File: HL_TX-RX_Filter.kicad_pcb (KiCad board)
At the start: 2 copper layers, 100 x 100 mm, 184 parts, among them J1 To Antenna, J2 From Tx, J3 ICSP, J4 Data In, J5 SCL SDA, J6 To Rx in, Q1 2N7002, Q2 2N7002, Q3 2N7002, Q4 2N7002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

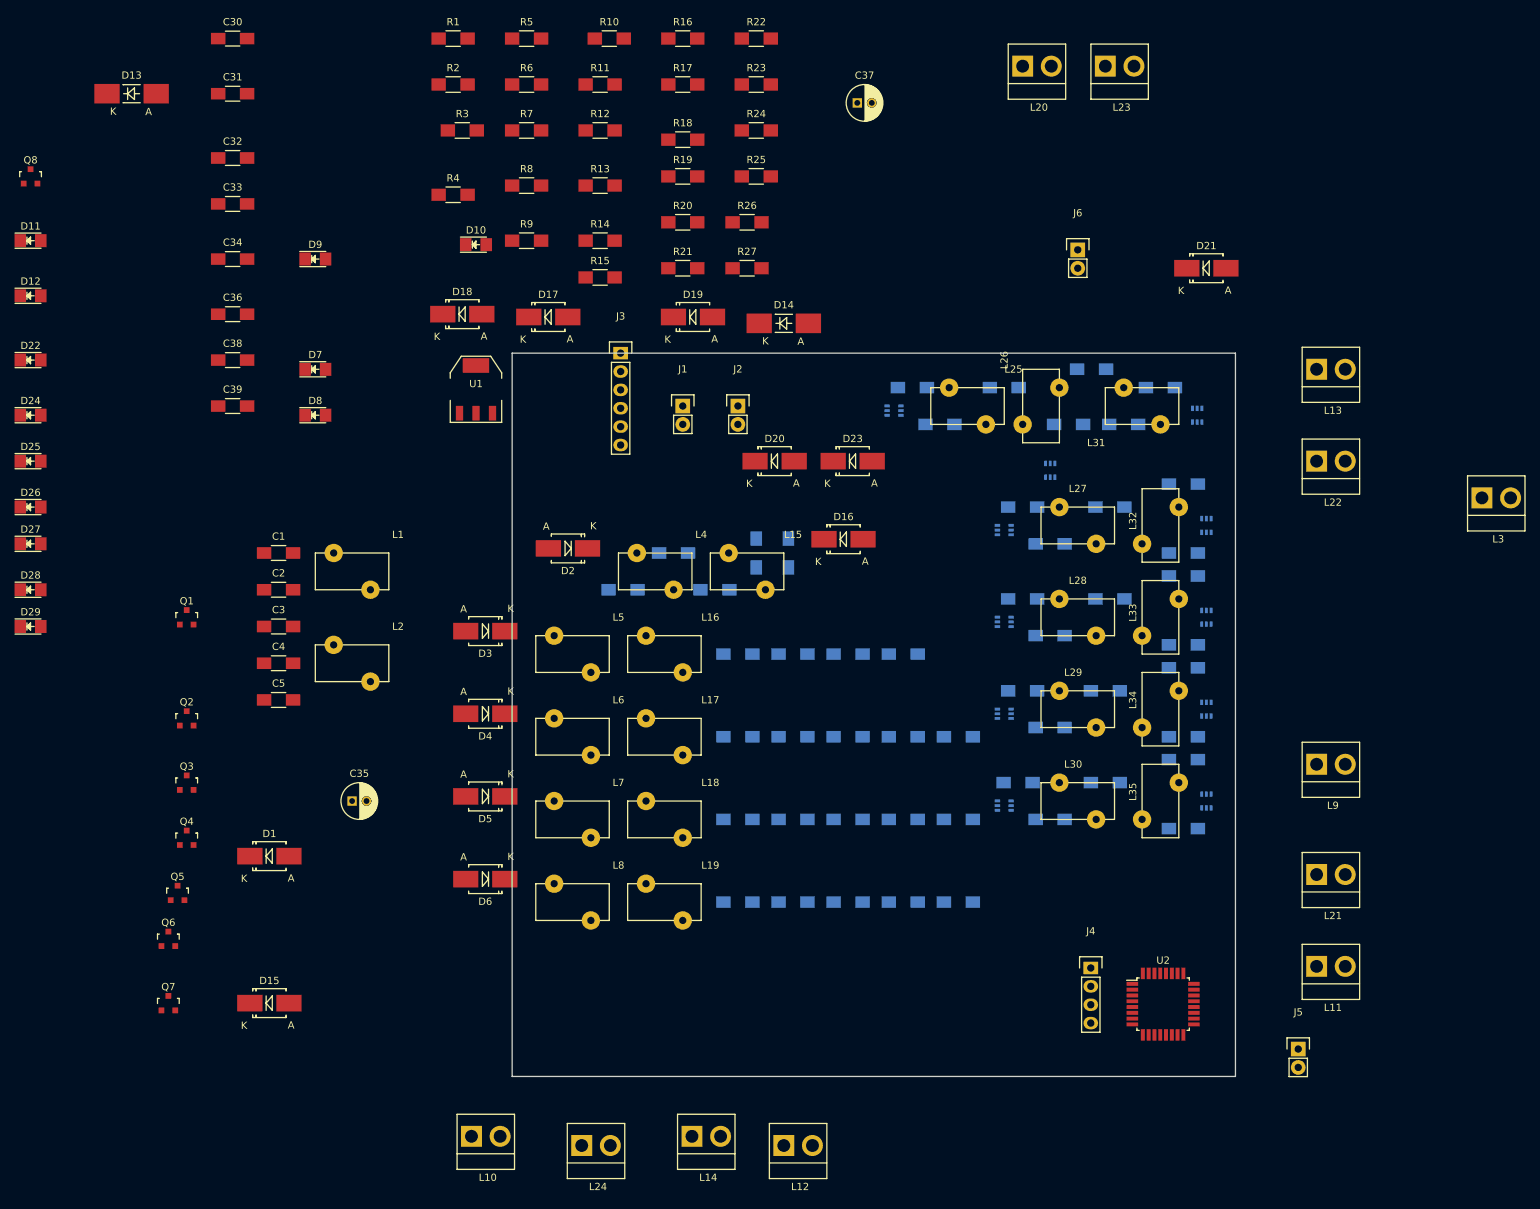
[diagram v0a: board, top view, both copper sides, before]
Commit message: Resized toroids and M7 diodes
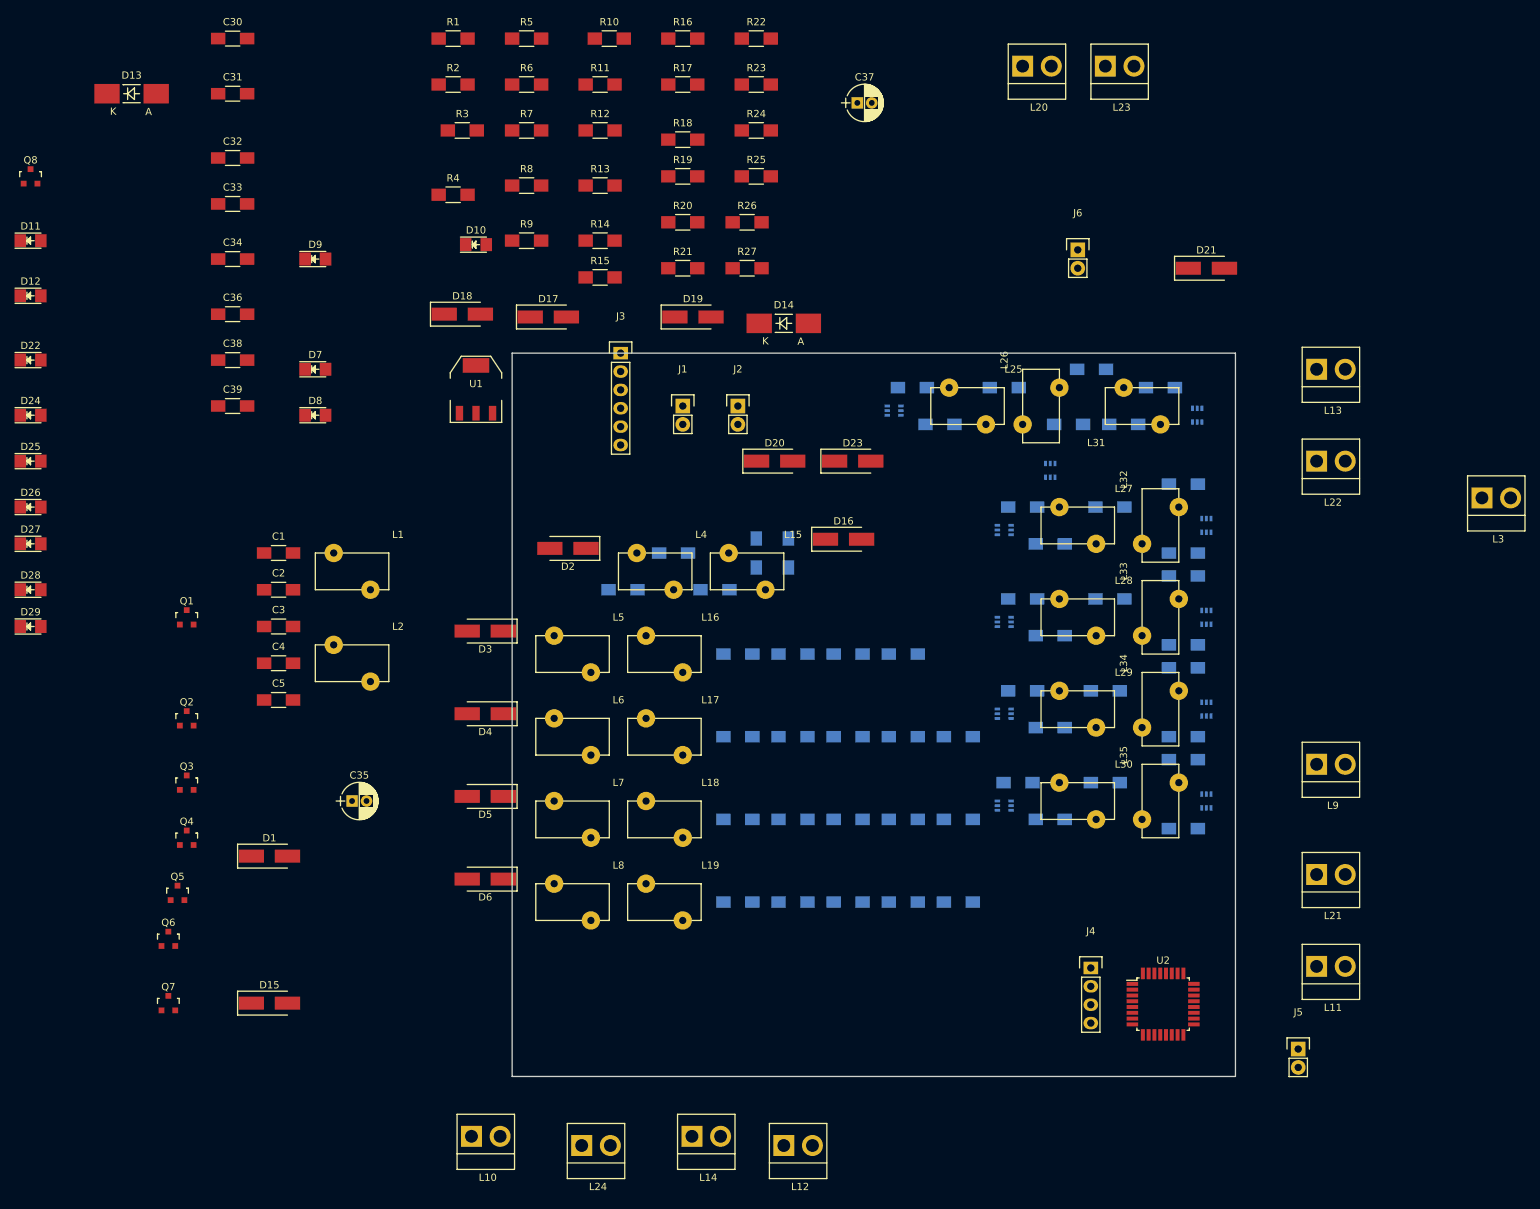
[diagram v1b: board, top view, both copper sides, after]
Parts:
- C35, C37: footprint Capacitors_ThroughHole:C_Radial_D5_L11_P2 -> Capacitors_THT:CP_Radial_D5.0mm_P2.00mm
- D1, D15, D16, D17, D18, D19, D2, D20, D21, D23, D3, D4, D5, D6: footprint Diodes_SMD:SMB_Handsoldering -> Diodes_SMD:D_SMA_Handsoldering
- L1, L15, L16, L17, L18, L19, L2, L25, L26, L27, L28, L29, L30, L31, L32, L33, L34, L35, L4, L5, L6, L7, L8: footprint Inductors:Toroid_T37_Vertical -> Inductors_G:Toroid_T37_Vertical

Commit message: Work on Tx Filter layout
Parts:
- moved C20 42.7 mm to (167.6, 144.1)
- moved C10 42.5 mm to (156.8, 144.1)
- moved C17 35.3 mm to (153.7, 105.4)
- moved C7 34.4 mm to (140.3, 105.4), turned to 180 degrees
- moved C15 16.6 mm to (147.3, 100.3)
- moved D3 11.6 mm to (132.7, 100.3)
- moved L16 11.5 mm to (152.4, 105.4)
- moved L5 11.5 mm to (139.7, 105.4)
- moved C25 3.24 mm to (175.9, 102.2)
- moved C16 0.63 mm to (153.7, 92.7)
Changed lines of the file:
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@@
-(kicad_pcb (version 4) (host pcbnew 4.0.6-e0-6349~53~ubuntu14.04.1)
+(kicad_pcb (version 4) (host pcbnew 4.0.6-e0-6349~53~ubuntu16.04.1)
   (general
     (links 329)
     (no_connects 329)
-    (area 124.924999 59.924999 225.075001 160.075001)
+    (area 55.315238 13.235 265.505001 176.32)
     (thickness 1.6)
     (drawings 4)
@@
   )
   (module Capacitors_SMD:C_1206_HandSoldering placed (layer B.Cu)
-    (at 156.21 135.89)
+    (at 140.335 105.41 180)
     (descr "Capacitor SMD 1206, hand soldering")
     (tags "capacitor 1206")
     (attr smd)
-    (fp_text reference C7 (at 0 2.3) (layer B.SilkS)
+    (fp_text reference C7 (at 0 2.3 180) (layer B.SilkS)
       (effects (font (size 1 1) (thickness 0.15)) (justify mirror))
     )
-    (fp_text value 150p (at 0 -2.3) (layer B.Fab)
+    (fp_text value 150p (at 0 -2.3 180) (layer B.Fab)
       (effects (font (size 1 1) (thickness 0.15)) (justify mirror))
     )
@@
     (fp_line (start 1 1.025) (end -1 1.025) (layer B.SilkS) (width 0.15))
     (fp_line (start -1 -1.025) (end 1 -1.025) (layer B.SilkS) (width 0.15))
-    (pad 1 smd rect (at -2 0) (size 2 1.6) (layers B.Cu B.Paste B.Mask)
+    (pad 1 smd rect (at -2 0 180) (size 2 1.6) (layers B.Cu B.Paste B.Mask)
       (net 6 "Net-(C12-Pad1)"))
-    (pad 2 smd rect (at 2 0) (size 2 1.6) (layers B.Cu B.Paste B.Mask)
+    (pad 2 smd rect (at 2 0 180) (size 2 1.6) (layers B.Cu B.Paste B.Mask)
       (net 4 GND))
     (model Capacitors_SMD.3dshapes/C_1206_HandSoldering.wrl
@@
   )
   (module Capacitors_SMD:C_1206_HandSoldering placed (layer B.Cu)
-    (at 156.21 101.6)
+    (at 156.845 144.145)
     (descr "Capacitor SMD 1206, hand soldering")
     (tags "capacitor 1206")
@@
   )
   (module Capacitors_SMD:C_1206_HandSoldering placed (layer B.Cu)
-    (at 163.83 101.6)
+    (at 147.32 100.33)
     (descr "Capacitor SMD 1206, hand soldering")
     (tags "capacitor 1206")
@@
   )
   (module Capacitors_SMD:C_1206_HandSoldering placed (layer B.Cu)
-    (at 153.035 92.71)
+    (at 153.67 92.71)
     (descr "Capacitor SMD 1206, hand soldering")
     (tags "capacitor 1206")
@@
   )
   (module Capacitors_SMD:C_1206_HandSoldering placed (layer B.Cu)
-    (at 171.45 135.89)
+    (at 153.67 105.41)
     (descr "Capacitor SMD 1206, hand soldering")
     (tags "capacitor 1206")
@@
   )
   (module Capacitors_SMD:C_1206_HandSoldering placed (layer B.Cu)
-    (at 171.45 101.6)
+    (at 167.64 144.145)
     (descr "Capacitor SMD 1206, hand soldering")
     (tags "capacitor 1206")
@@
     (tags "capacitor 1206")
     (attr smd)
-    (fp_text reference C21 (at 0 2.3 90) (layer B.SilkS)
+    (fp_text reference C21 (at -0.635 1.905 90) (layer B.SilkS)
       (effects (font (size 1 1) (thickness 0.15)) (justify mirror))
     )
@@
   )
   (module Capacitors_SMD:C_1206_HandSoldering placed (layer B.Cu)
-    (at 179.07 101.6)
+    (at 175.895 102.235)
     (descr "Capacitor SMD 1206, hand soldering")
     (tags "capacitor 1206")
@@
     (tags "capacitor 1206")
     (attr smd)
-    (fp_text reference C26 (at 0 2.3 270) (layer B.SilkS)
+    (fp_text reference C26 (at 3.175 -2.54 270) (layer B.SilkS)
       (effects (font (size 1 1) (thickness 0.15)) (justify mirror))
     )
@@
   )
   (module Inductors_G:Toroid_T37_Vertical (layer F.Cu)
-    (at 128.27 104.14)
+    (at 139.7 105.41)
     (descr "Toroid, Coil, Choke,  5mm x 10mm, Vertical, Inductor, Drossel, Thruhole,")
     (tags "Toroid, Coil, Choke, 5mm x 10mm, Vertical, Inductor, Drossel, Thruhole,")
@@
   )
   (module Inductors_G:Toroid_T37_Vertical (layer F.Cu)
-    (at 140.97 104.14)
+    (at 152.4 105.41)
     (descr "Toroid, Coil, Choke,  5mm x 10mm, Vertical, Inductor, Drossel, Thruhole,")
     (tags "Toroid, Coil, Choke, 5mm x 10mm, Vertical, Inductor, Drossel, Thruhole,")
@@
   )
   (module Diodes_SMD:D_SMA_Handsoldering (layer F.Cu)
-    (at 121.285 98.425 180)
+    (at 132.715 100.33 180)
     (descr "Diode SMA (DO-214AC) Handsoldering")
     (tags "Diode SMA (DO-214AC) Handsoldering")

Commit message: More Tx filter layout
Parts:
- C30: moved to B.Cu
- moved C30 144.1 mm to (163.2, 138.4), turned to 270 degrees
- moved D18 77.3 mm to (170.8, 111.1)
- moved D19 71.9 mm to (170.8, 123.8)
- moved D20 61.7 mm to (170.8, 135.9)
- moved D17 59.6 mm to (170.8, 98.4)
- moved C27 42.6 mm to (163.2, 100.3), turned to 270 degrees
- moved C22 41.0 mm to (158.8, 100.3), turned to 90 degrees
- moved C25 40.1 mm to (158.8, 138.4), turned to 90 degrees
- moved C12 39.2 mm to (147.3, 100.3)
- moved C15 38.1 mm to (147.3, 138.4)
- moved C29 26.7 mm to (163.2, 125.7), turned to 270 degrees
- moved C28 26.1 mm to (163.2, 113.0), turned to 270 degrees
- moved C19 25.1 mm to (153.7, 130.8)
- moved C24 24.0 mm to (158.8, 125.7), turned to 90 degrees
- moved C9 23.8 mm to (140.3, 130.8), turned to 180 degrees
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
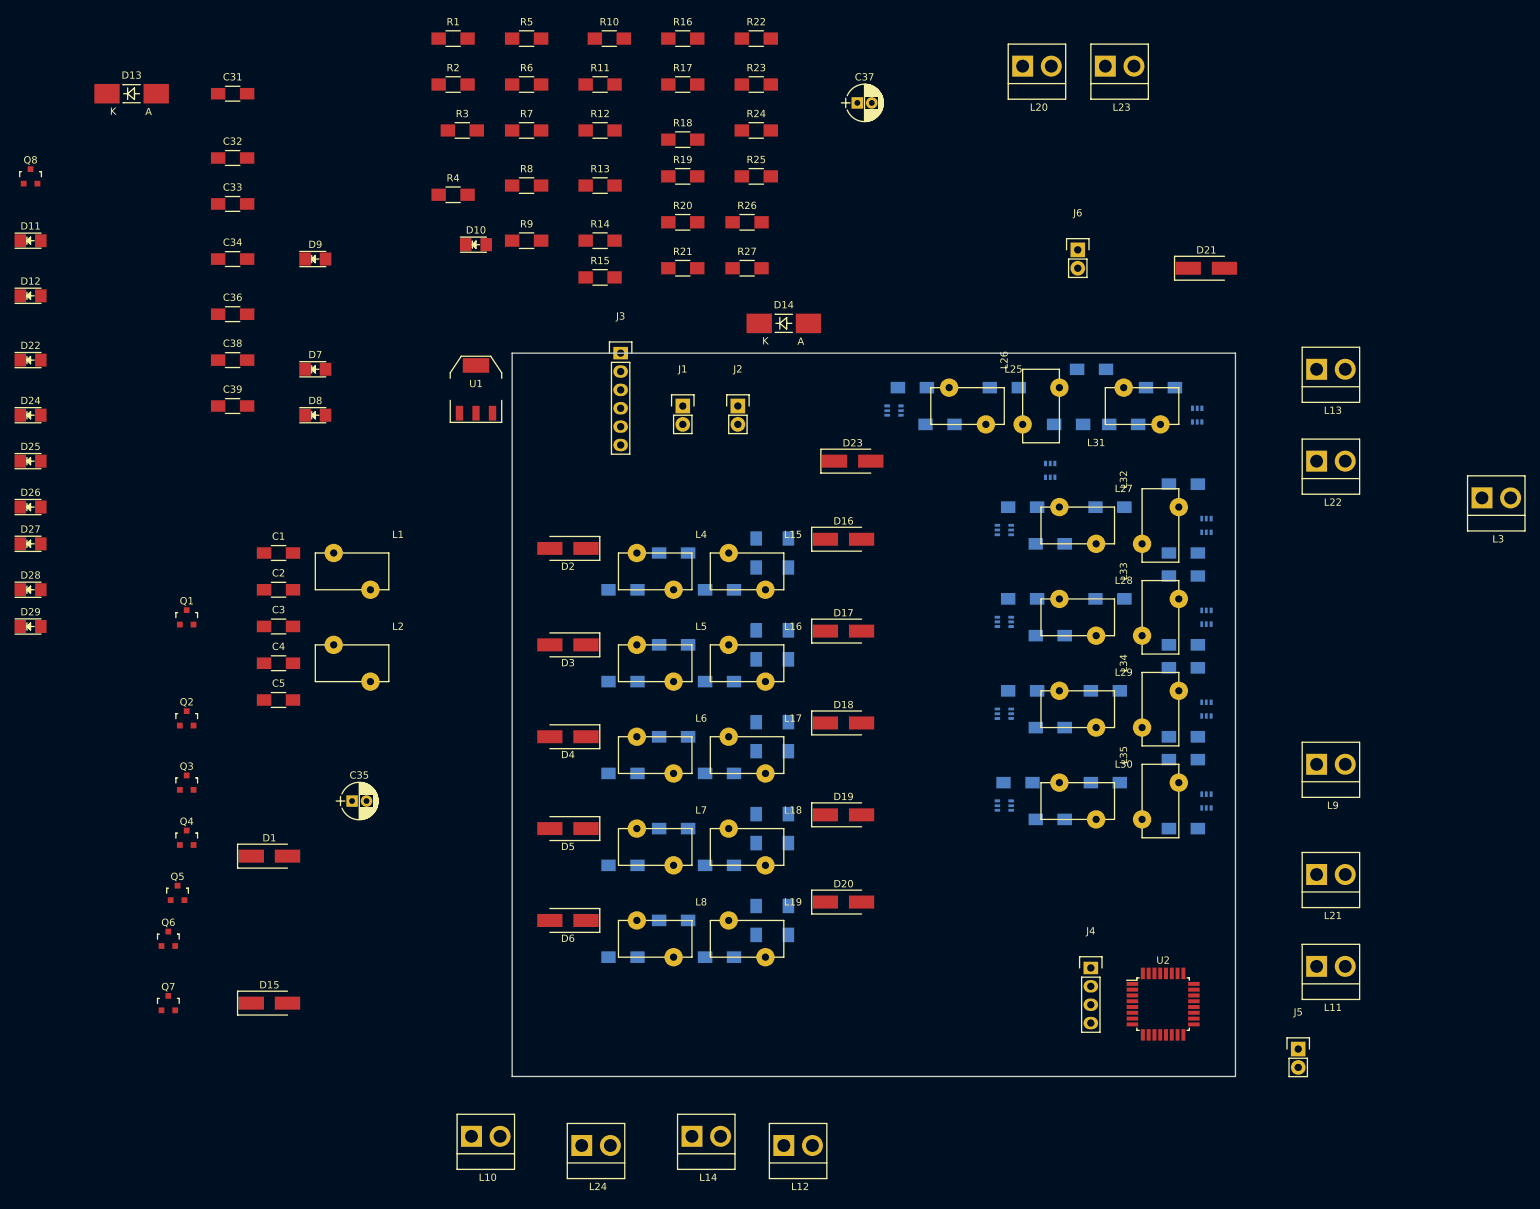
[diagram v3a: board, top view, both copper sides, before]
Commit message: More Tx layout and choke footprint mods
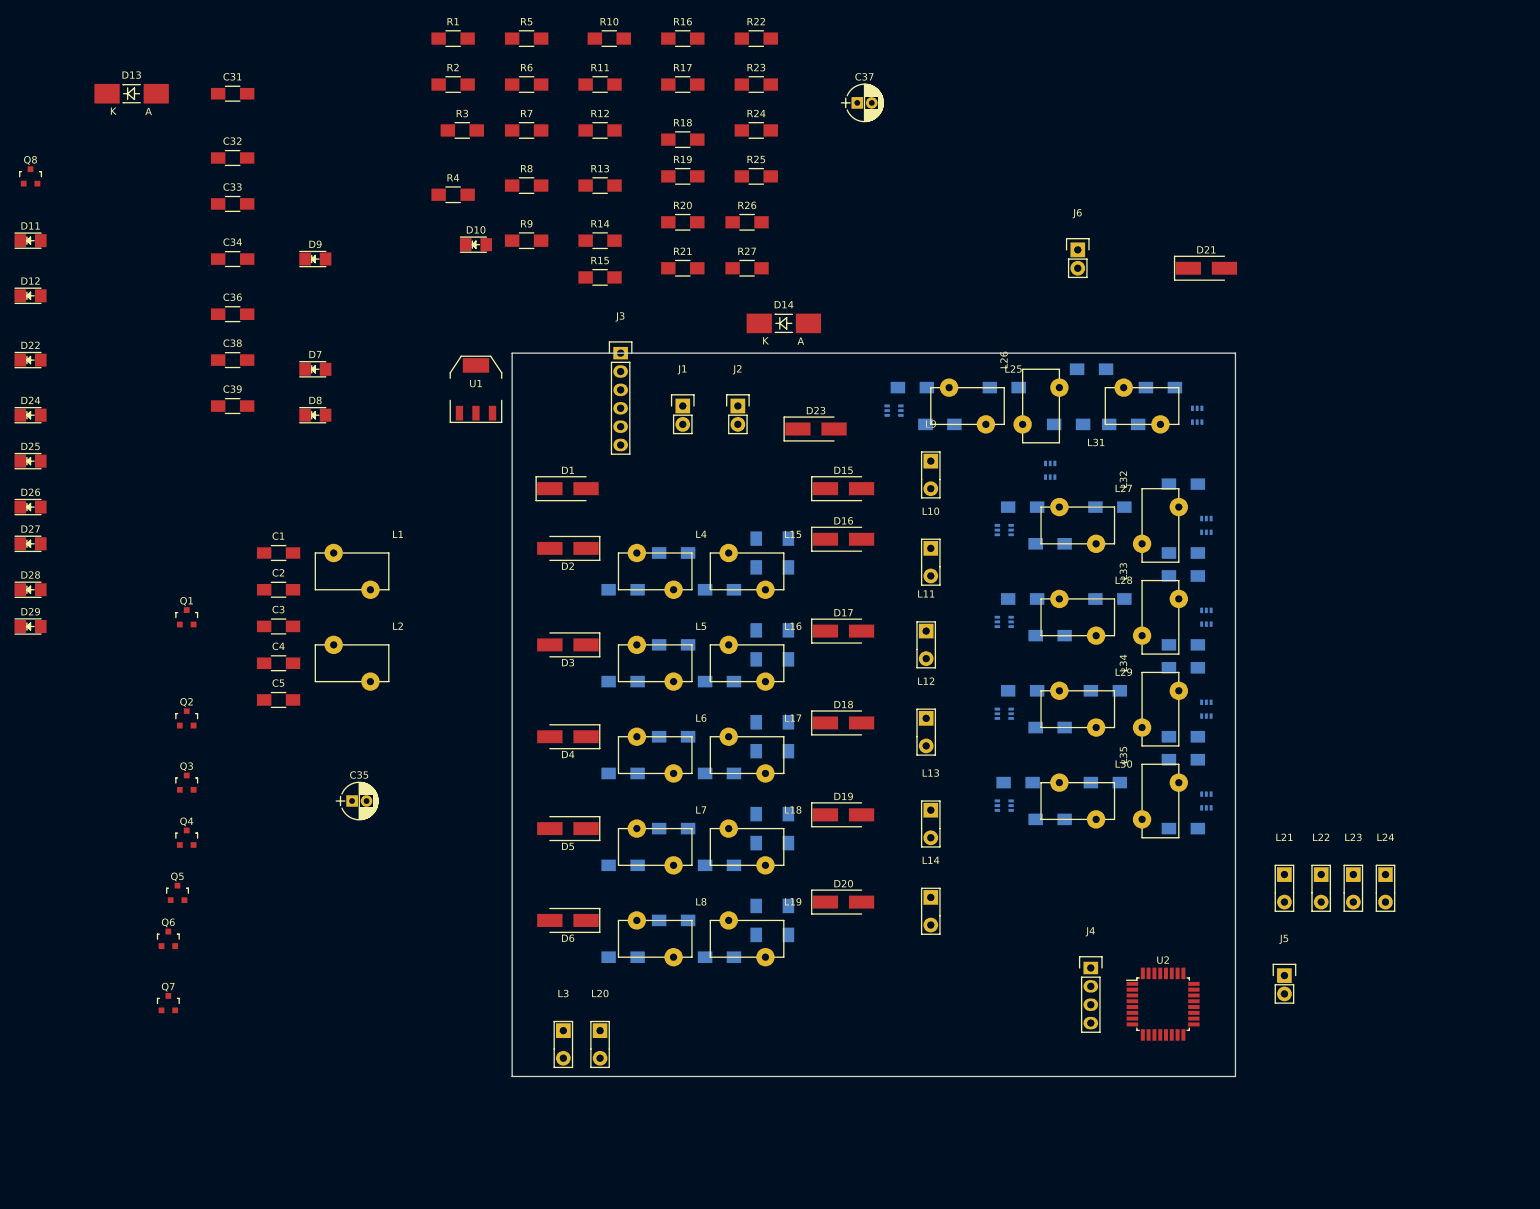
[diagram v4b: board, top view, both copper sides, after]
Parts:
- L10, L11, L12, L13, L14, L20, L21, L22, L23, L24, L3, L9: footprint Pin_Headers:Pin_Header_Straight_1x02_Pitch3.96mm_Friction_Lock -> Inductors_G:BalunCoreChoke
- moved L3 146.8 mm to (132.1, 153.7)
- moved L20 145.6 mm to (137.2, 153.7)
- moved L24 117.3 mm to (245.7, 132.1)
- moved L23 116.9 mm to (241.3, 132.1)
- moved D15 106.6 mm to (170.8, 78.7)
- moved L10 103.1 mm to (182.9, 87.0)
- moved L13 81.0 mm to (182.9, 123.2)
- moved L11 71.1 mm to (182.2, 98.4)
- moved L9 67.8 mm to (182.9, 74.9)
- moved D1 65.5 mm to (132.7, 78.7)
- moved L12 62.2 mm to (182.2, 110.5)
- moved L22 57.2 mm to (236.9, 132.1)
- moved L14 46.7 mm to (182.9, 135.3)
- moved J5 10.3 mm to (231.8, 146.1)
- moved D23 6.75 mm to (167.0, 70.5)
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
